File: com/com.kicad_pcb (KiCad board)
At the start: 2 copper layers, 50 x 50 mm, 69 parts, among them J1 Conn_01x02, J3 Conn_01x04, J4 USB_B_Micro, J5 Conn_01x04, J6 Conn_01x01, J7 Conn_01x01, J8 Conn_01x01, J9 Conn_01x01, SW1 SW_DIP_x08, U1 SPSGRF-868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

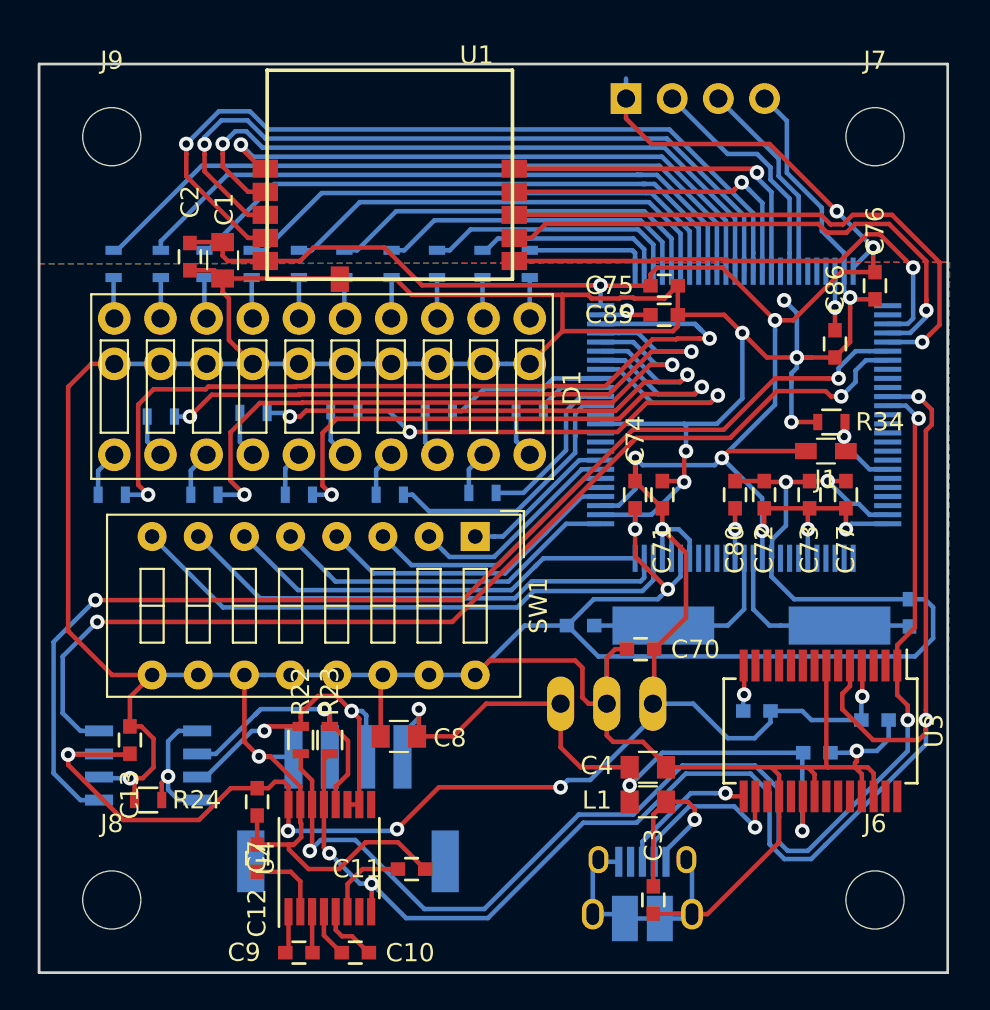
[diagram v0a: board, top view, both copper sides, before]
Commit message: com board: silkscreen and 3d
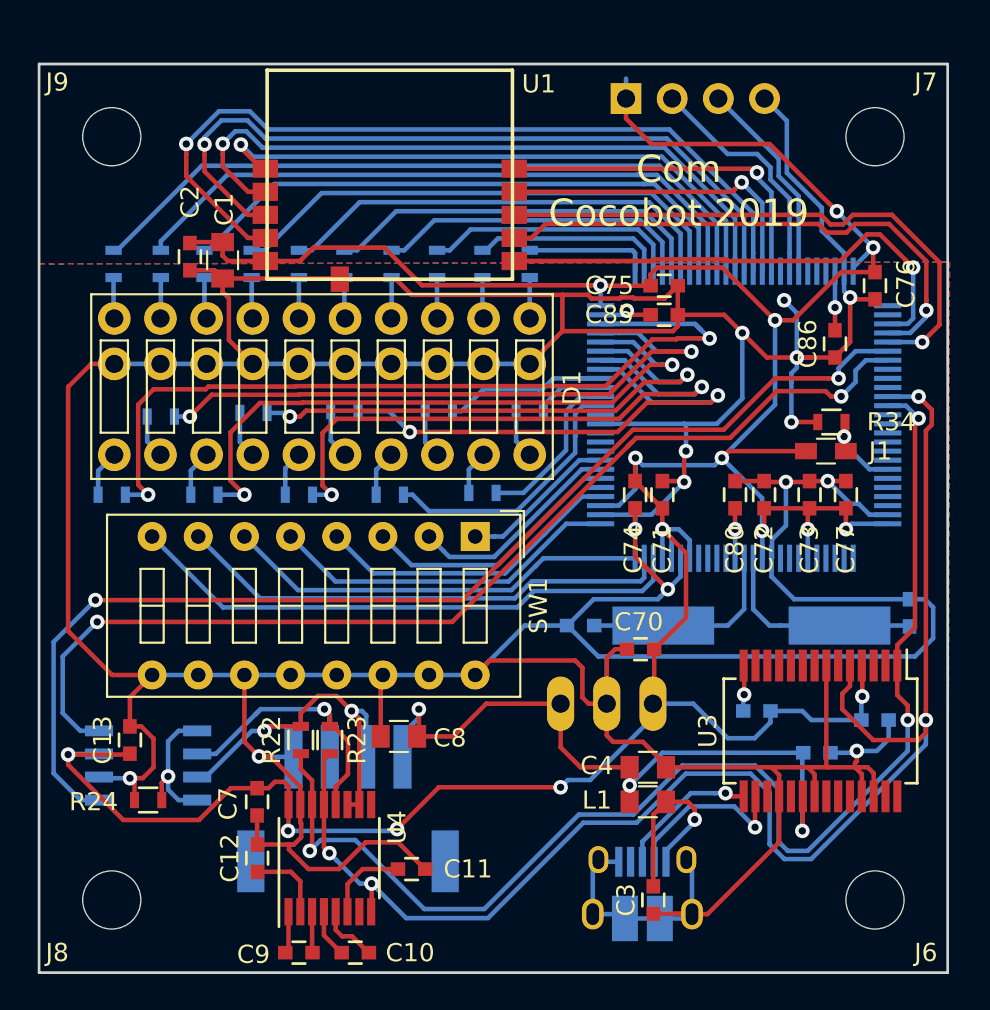
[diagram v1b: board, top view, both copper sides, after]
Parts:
- J4: footprint Connectors:USB_Micro-B_10103594-0001LF -> espitall:USB_Micro-B_10103594-0001LF
- J5: footprint Connectors_JST:JST_PH_S4B-PH-SM4-TB_04x2.00mm_Angled -> espitall:JST_PH_S4B-PH-SM4-TB_04x2.00mm_Angled
- SW1: footprint Buttons_Switches_THT:SW_DIP_x8_W7.62mm_Slide -> espitall:SW_DIP_x8_W7.62mm_Slide
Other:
- board text added: "Com Cocobot 2019"

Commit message: create specific connector for CAN bus
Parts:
- removed J5: Conn_01x04, espitall:JST_PH_S4B-PH-SM4-TB_04x2.00mm_Angled
- added J2: CocobotCAN, espitall:JST_PH_S4B-PH-SM4-TB_04x2.00mm_Angled, B.Cu at (67.0, 91.0)
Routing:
- net GND: track 353.4 -> 373.7 mm

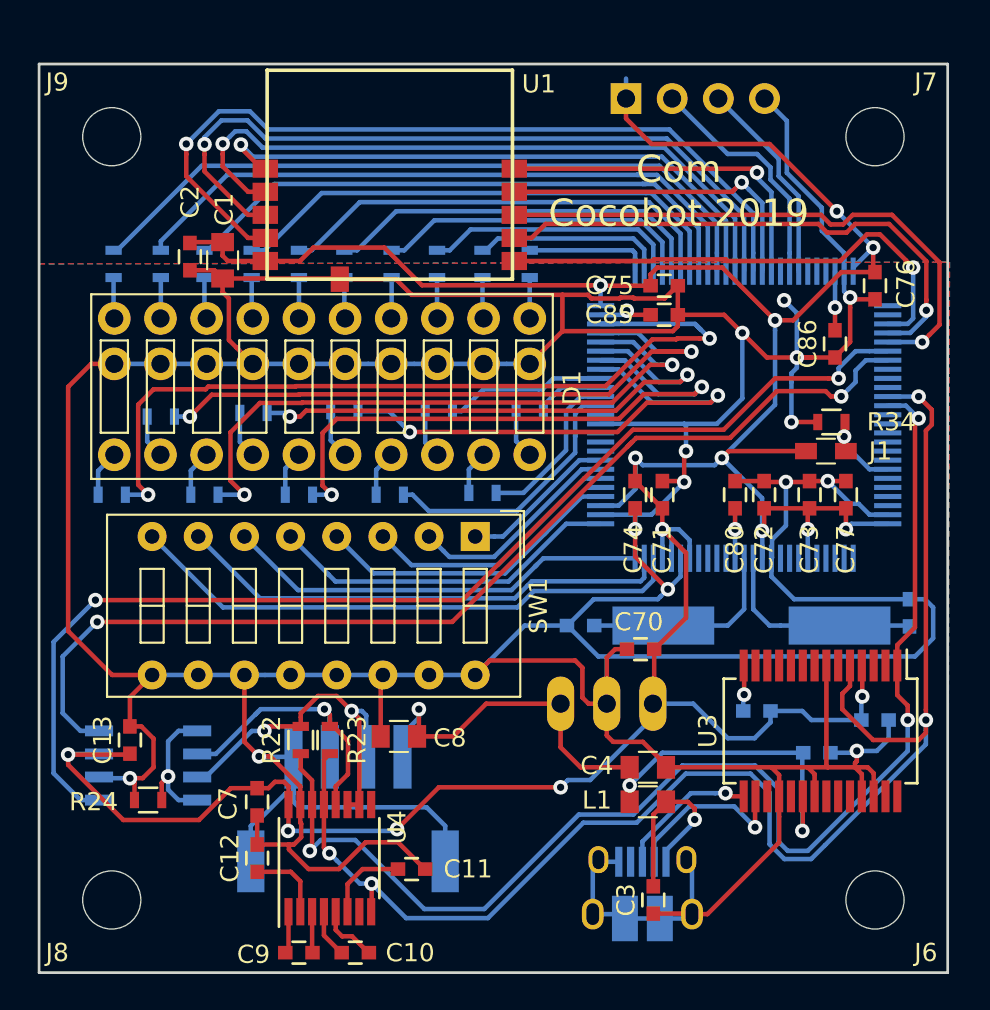
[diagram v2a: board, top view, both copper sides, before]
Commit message: add electrical protection on CAN bus
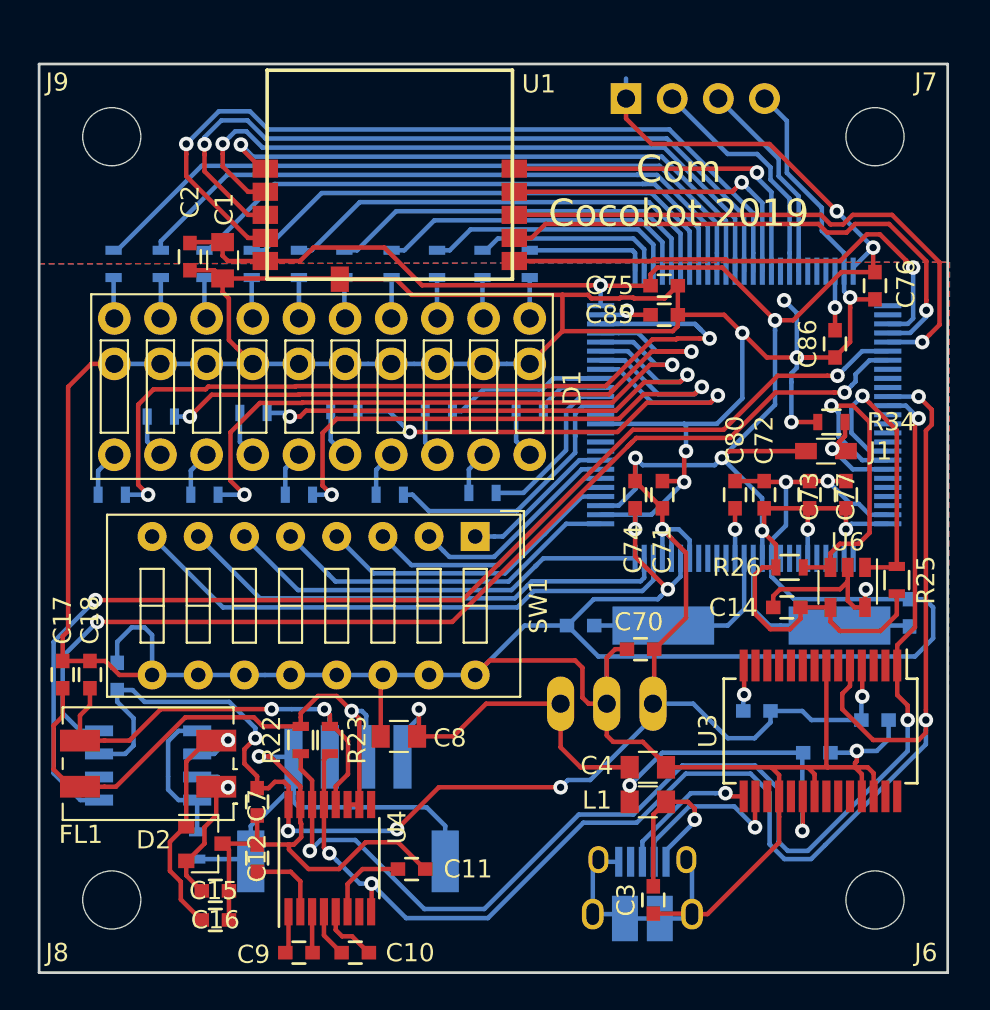
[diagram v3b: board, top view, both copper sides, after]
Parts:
- added C14: 100n, espitall:C_0603, F.Cu at (91.2, 79.9)
- added C15: C, espitall:C_0603, F.Cu at (59.7, 95.5)
- added C16: C, espitall:C_0603, F.Cu at (59.7, 97.1)
- added C17: C, espitall:C_0603, F.Cu at (51.3, 83.6)
- added C18: C, espitall:C_0603, F.Cu at (52.8, 83.6)
- added D2: NUP2105LT1G, espitall:SOT-23, F.Cu at (59.1, 92.9)
- added FL1: DR331-113BE, espitall:DR331, F.Cu at (56.0, 88.5)
- added R25: 2k2, espitall:R_0603, F.Cu at (97.2, 78.4)
- added R26: 2k2, espitall:R_0603, F.Cu at (91.3, 77.7)
- added U6: 24LC64T-I, espitall:SOT-23-5, F.Cu at (94.5, 78.8)
- C13, R24: moved to B.Cu
- moved R24 3.68 mm to (58.7, 93.0), turned to 270 degrees
- moved C13 3.57 mm to (54.3, 83.7)
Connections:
- J4 pad 4: (no net) -> Net-(J4-Pad4)
- J6 pad 1: (no net) -> Net-(J6-Pad1)
- J7 pad 1: (no net) -> Net-(J7-Pad1)
- J8 pad 1: (no net) -> Net-(J8-Pad1)
- J9 pad 1: (no net) -> Net-(J9-Pad1)
- U3 pad 10: (no net) -> Net-(U3-Pad10)
- U3 pad 11: (no net) -> Net-(U3-Pad11)
- U3 pad 12: (no net) -> Net-(U3-Pad12)
- U3 pad 13: (no net) -> Net-(U3-Pad13)
- U3 pad 17: (no net) -> Net-(U3-Pad17)
- U3 pad 19: (no net) -> Net-(U3-Pad19)
- U3 pad 2: (no net) -> Net-(U3-Pad2)
- U3 pad 22: (no net) -> Net-(U3-Pad22)
- U3 pad 23: (no net) -> Net-(U3-Pad23)
- U3 pad 27: (no net) -> Net-(U3-Pad27)
- U3 pad 28: (no net) -> Net-(U3-Pad28)
- U3 pad 3: (no net) -> Net-(U3-Pad3)
- U3 pad 6: (no net) -> Net-(U3-Pad6)
- U3 pad 9: (no net) -> Net-(U3-Pad9)
- U4 pad 7: (no net) -> Net-(U4-Pad7)
- U4 pad 9: (no net) -> Net-(U4-Pad9)
- U5 pad 6: /CAN/can_l -> Net-(C16-Pad1)
- U5 pad 7: /CAN/can_h -> Net-(C15-Pad1)
- U8 pad 1: (no net) -> Net-(U8-Pad1)
- U8 pad 15: (no net) -> Net-(U8-Pad15)
- U8 pad 16: (no net) -> Net-(U8-Pad16)
- U8 pad 17: (no net) -> Net-(U8-Pad17)
- U8 pad 18: (no net) -> Net-(U8-Pad18)
- U8 pad 2: (no net) -> Net-(U8-Pad2)
- U8 pad 3: (no net) -> Net-(U8-Pad3)
- U8 pad 30: (no net) -> Net-(U8-Pad30)
- U8 pad 34: (no net) -> Net-(U8-Pad34)
- U8 pad 35: (no net) -> Net-(U8-Pad35)
- U8 pad 36: (no net) -> Net-(U8-Pad36)
- U8 pad 38: (no net) -> Net-(U8-Pad38)
- U8 pad 4: (no net) -> Net-(U8-Pad4)
- U8 pad 5: (no net) -> Net-(U8-Pad5)
- U8 pad 67: (no net) -> Net-(U8-Pad67)
- U8 pad 7: (no net) -> Net-(U8-Pad7)
- U8 pad 70: (no net) -> Net-(U8-Pad70)
- U8 pad 71: (no net) -> Net-(U8-Pad71)
- U8 pad 72: (no net) -> Net-(U8-Pad72)
- U8 pad 76: (no net) -> Net-(U8-Pad76)
- U8 pad 77: (no net) -> Net-(U8-Pad77)
- U8 pad 8: (no net) -> Net-(U8-Pad8)
- U8 pad 83: (no net) -> Net-(U8-Pad83)
- U8 pad 84: (no net) -> Net-(U8-Pad84)
- U8 pad 85: (no net) -> Net-(U8-Pad85)
- U8 pad 88: (no net) -> Net-(U8-Pad88)
- U8 pad 89: (no net) -> Net-(U8-Pad89)
- U8 pad 9: (no net) -> Net-(U8-Pad9)
- U8 pad 90: (no net) -> Net-(U8-Pad90)
- U8 pad 91: (no net) -> Net-(U8-Pad91)
- U8 pad 92: (no net) -> Net-(R25-Pad2)
- U8 pad 93: (no net) -> Net-(R26-Pad2)
- U8 pad 95: (no net) -> Net-(U8-Pad95)
- U8 pad 96: (no net) -> Net-(U8-Pad96)
- U8 pad 97: (no net) -> Net-(U8-Pad97)
- U8 pad 98: (no net) -> Net-(U8-Pad98)
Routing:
- net Net-(R26-Pad2): track 0.00 -> 18.6 mm, vias 0 -> 1
- net +3V3: track 191.2 -> 208.2 mm
- net Net-(R25-Pad2): track 0.00 -> 16.6 mm, vias 0 -> 1
- net Net-(C16-Pad1): track 0.00 -> 15.3 mm, vias 0 -> 1
- net /CAN/can_h: track 20.3 -> 33.9 mm, vias 2 -> 1
- net Net-(C15-Pad1): track 0.00 -> 11.0 mm, vias 0 -> 1
- net GND: track 373.7 -> 383.9 mm
- net /CAN/can_l: track 19.3 -> 28.3 mm, vias 1 -> 2
- net /uc/BOOT0_3v3: track 5.04 -> 6.09 mm
- net Net-(R24-Pad1): track 7.78 -> 8.08 mm, vias 1 -> 0

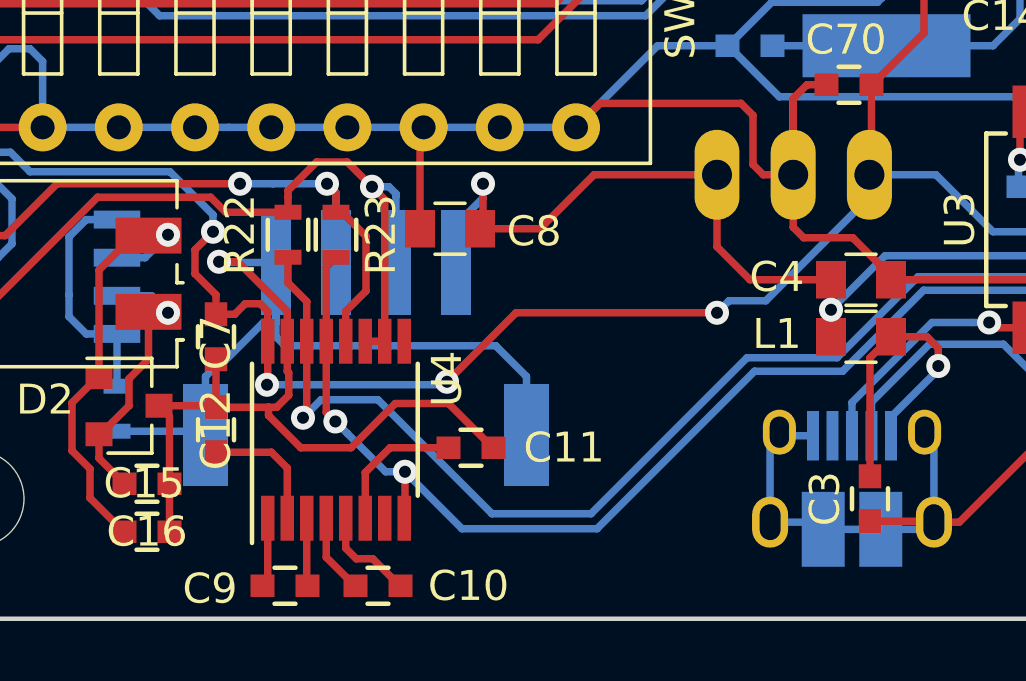
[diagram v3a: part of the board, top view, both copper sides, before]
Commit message: update com board with new CAN connector
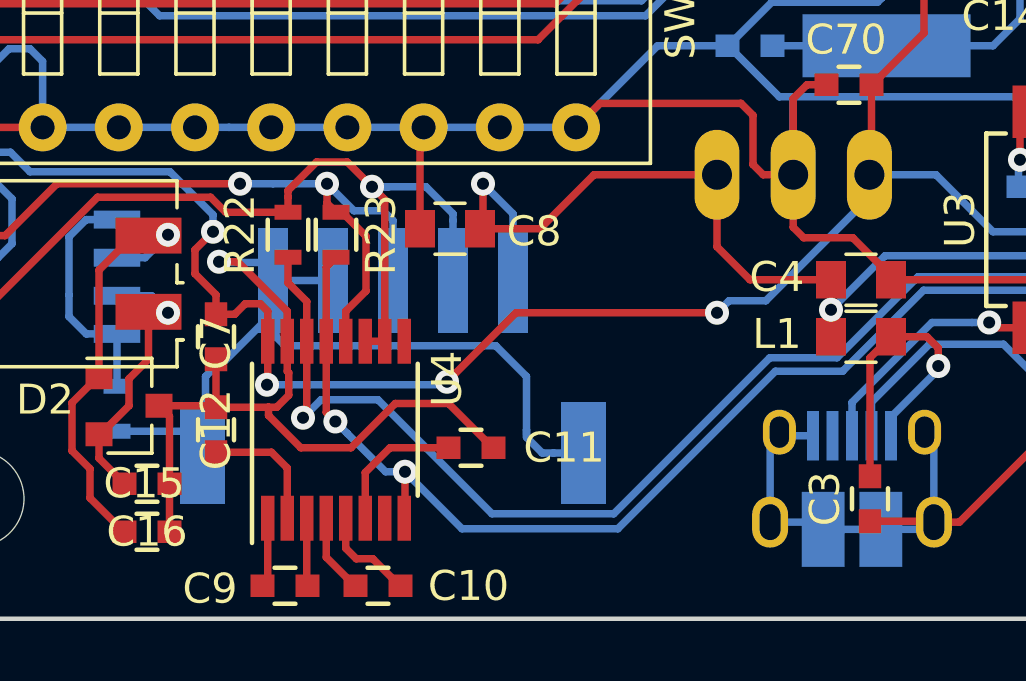
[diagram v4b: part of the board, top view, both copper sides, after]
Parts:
- J2: footprint espitall:JST_PH_S4B-PH-SM4-TB_04x2.00mm_Angled -> espitall:JST_PH_S5B-PH-SM4-TB_05x2.00mm_Angled
- moved J2 1.08 mm to (67.9, 91.6)
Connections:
- J4 pad 4: Net-(J4-Pad4) -> (no net)
- J6 pad 1: Net-(J6-Pad1) -> (no net)
- J7 pad 1: Net-(J7-Pad1) -> (no net)
- J8 pad 1: Net-(J8-Pad1) -> (no net)
- J9 pad 1: Net-(J9-Pad1) -> (no net)
- U3 pad 10: Net-(U3-Pad10) -> (no net)
- U3 pad 11: Net-(U3-Pad11) -> (no net)
- U3 pad 12: Net-(U3-Pad12) -> (no net)
- U3 pad 13: Net-(U3-Pad13) -> (no net)
- U3 pad 17: Net-(U3-Pad17) -> (no net)
- U3 pad 19: Net-(U3-Pad19) -> (no net)
- U3 pad 2: Net-(U3-Pad2) -> (no net)
- U3 pad 22: Net-(U3-Pad22) -> (no net)
- U3 pad 23: Net-(U3-Pad23) -> (no net)
- U3 pad 27: Net-(U3-Pad27) -> (no net)
- U3 pad 28: Net-(U3-Pad28) -> (no net)
- U3 pad 3: Net-(U3-Pad3) -> (no net)
- U3 pad 6: Net-(U3-Pad6) -> (no net)
- U3 pad 9: Net-(U3-Pad9) -> (no net)
- U4 pad 7: Net-(U4-Pad7) -> (no net)
- U4 pad 9: Net-(U4-Pad9) -> (no net)
- U8 pad 1: Net-(U8-Pad1) -> (no net)
- U8 pad 15: Net-(U8-Pad15) -> (no net)
- U8 pad 16: Net-(U8-Pad16) -> (no net)
- U8 pad 17: Net-(U8-Pad17) -> (no net)
- U8 pad 18: Net-(U8-Pad18) -> (no net)
- U8 pad 2: Net-(U8-Pad2) -> (no net)
- U8 pad 3: Net-(U8-Pad3) -> (no net)
- U8 pad 30: Net-(U8-Pad30) -> (no net)
- U8 pad 34: Net-(U8-Pad34) -> (no net)
- U8 pad 35: Net-(U8-Pad35) -> (no net)
- U8 pad 36: Net-(U8-Pad36) -> (no net)
- U8 pad 38: Net-(U8-Pad38) -> (no net)
- U8 pad 4: Net-(U8-Pad4) -> (no net)
- U8 pad 5: Net-(U8-Pad5) -> (no net)
- U8 pad 67: Net-(U8-Pad67) -> (no net)
- U8 pad 7: Net-(U8-Pad7) -> (no net)
- U8 pad 70: Net-(U8-Pad70) -> (no net)
- U8 pad 71: Net-(U8-Pad71) -> (no net)
- U8 pad 72: Net-(U8-Pad72) -> (no net)
- U8 pad 76: Net-(U8-Pad76) -> (no net)
- U8 pad 77: Net-(U8-Pad77) -> (no net)
- U8 pad 8: Net-(U8-Pad8) -> (no net)
- U8 pad 83: Net-(U8-Pad83) -> (no net)
- U8 pad 84: Net-(U8-Pad84) -> (no net)
- U8 pad 85: Net-(U8-Pad85) -> (no net)
- U8 pad 88: Net-(U8-Pad88) -> (no net)
- U8 pad 89: Net-(U8-Pad89) -> (no net)
- U8 pad 9: Net-(U8-Pad9) -> (no net)
- U8 pad 90: Net-(U8-Pad90) -> (no net)
- U8 pad 91: Net-(U8-Pad91) -> (no net)
- U8 pad 95: Net-(U8-Pad95) -> (no net)
- U8 pad 96: Net-(U8-Pad96) -> (no net)
- U8 pad 97: Net-(U8-Pad97) -> (no net)
- U8 pad 98: Net-(U8-Pad98) -> (no net)
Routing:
- net GND: track 383.9 -> 388.3 mm
- net /CAN/can_h: track 33.9 -> 36.6 mm
- net /Computer/5v: track 38.3 -> 38.9 mm
